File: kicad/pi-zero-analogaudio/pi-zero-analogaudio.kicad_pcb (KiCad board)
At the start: 2 copper layers, 30.5 x 26 mm, 13 parts, among them J1 Audio Out, J2 Pi Connector 2x5 Female, U1 STX-3120-3B

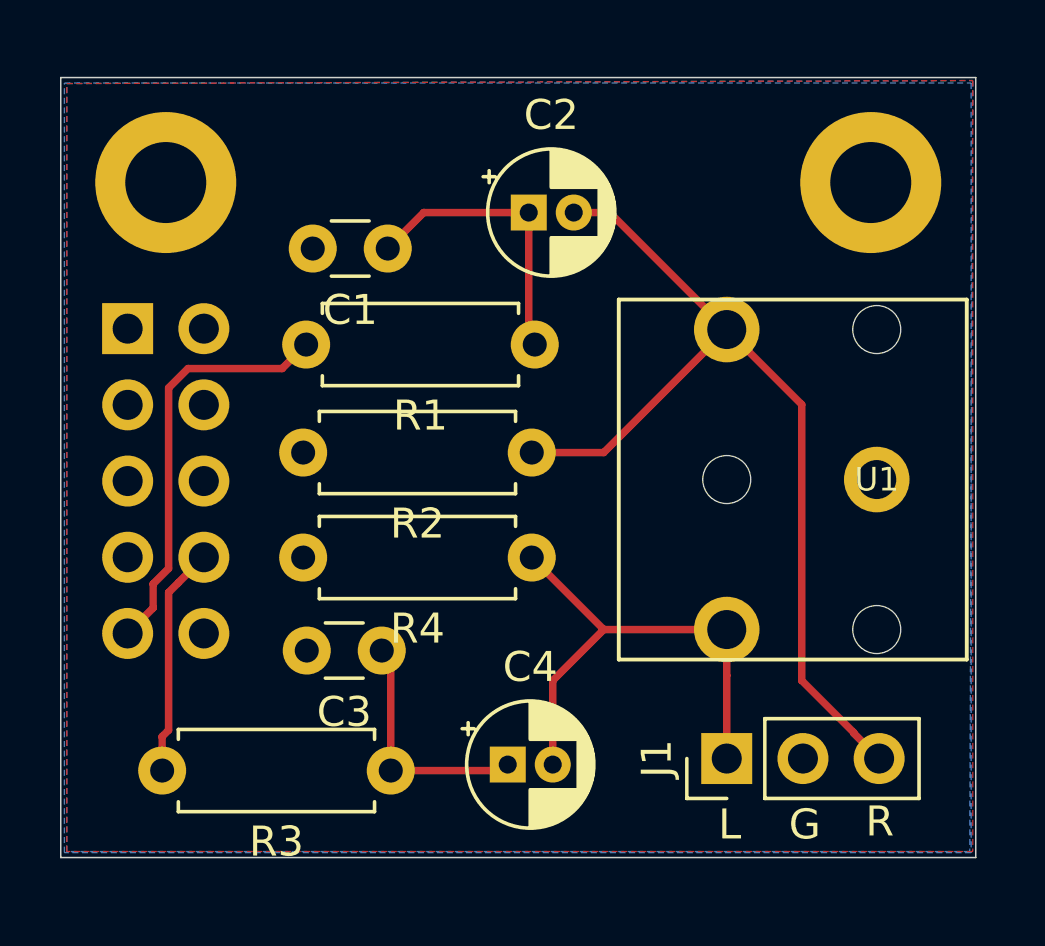
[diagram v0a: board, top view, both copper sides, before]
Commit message: Revision 8: replaced STX3120-3B with STX3120-5B
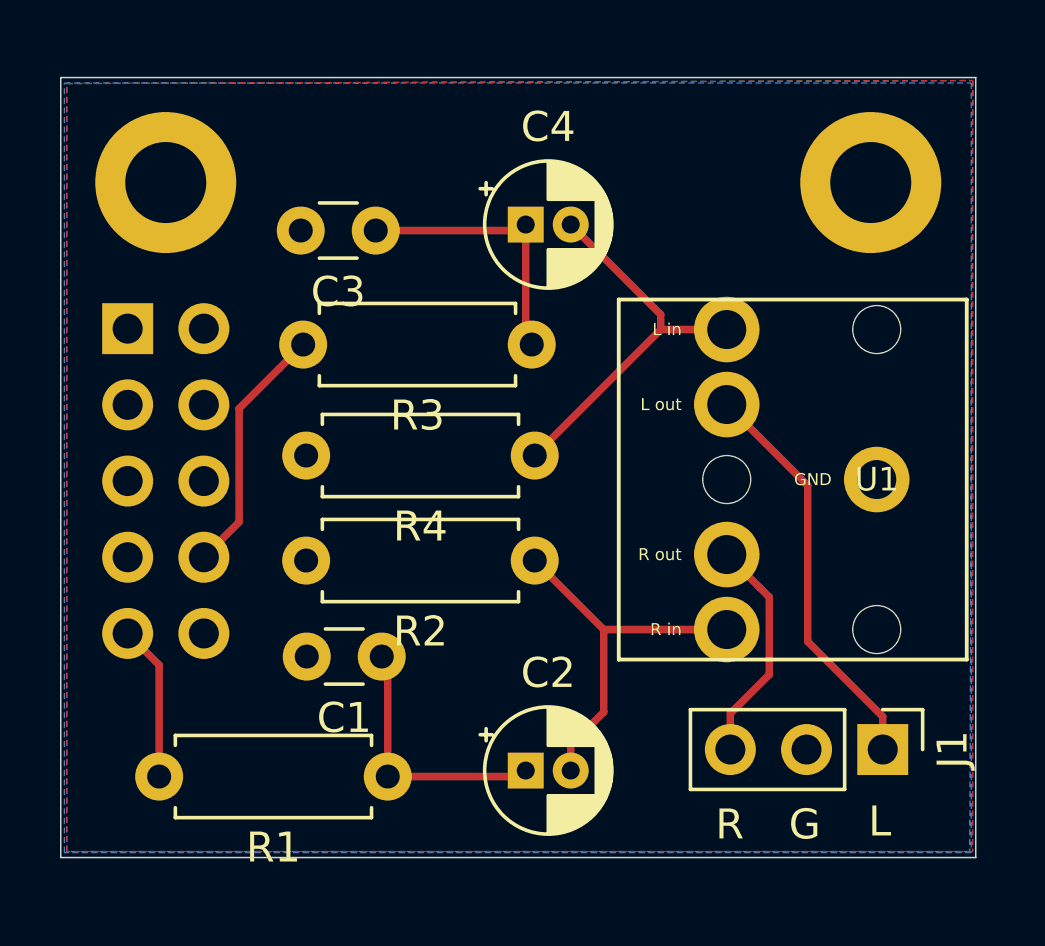
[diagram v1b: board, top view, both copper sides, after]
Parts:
- U1: value STX-3120-3B -> STX-3120-5B; footprint Download:STX-3120 -> Download:STX-3120-5B
- moved C2 18.6 mm to (102.5, 82.1)
- moved C4 18.0 mm to (102.5, 63.9)
- moved R1 15.2 mm to (97.9, 82.3)
- moved R3 15.0 mm to (102.7, 67.9)
- moved C3 14.0 mm to (97.5, 64.1)
- moved C1 13.6 mm to (97.7, 78.3)
- moved J1 5.21 mm to (114.4, 81.4), turned to 270 degrees
- moved R2 3.60 mm to (102.8, 75.1)
- moved R4 3.40 mm to (102.8, 71.6)
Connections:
- J1 pad 1: Net-(C4-Pad2) -> Net-(J1-Pad1)
- J1 pad 3: Net-(C2-Pad2) -> Net-(J1-Pad3)
- U1 pad 2: Net-(C2-Pad2) -> Net-(C4-Pad2)
- U1 pad 5: Net-(C4-Pad2) -> Net-(C2-Pad2)
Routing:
- net Net-(C2-Pad2): track 31.3 -> 12.5 mm
- net Net-(J1-Pad1): track 0.00 -> 13.7 mm
- net Net-(J2-Pad9): track 13.9 -> 5.20 mm
- net Net-(J1-Pad3): track 0.00 -> 7.62 mm
- net Net-(C4-Pad2): track 17.0 -> 12.9 mm
- net Net-(C3-Pad1): track 8.11 -> 9.17 mm
- net Net-(C1-Pad1): track 9.68 -> 8.77 mm
- net Net-(J2-Pad8): track 7.69 -> 8.46 mm
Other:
- board text added: "https://github.com/bablokb/pi-zero-analogaudio"

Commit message: added cutoff
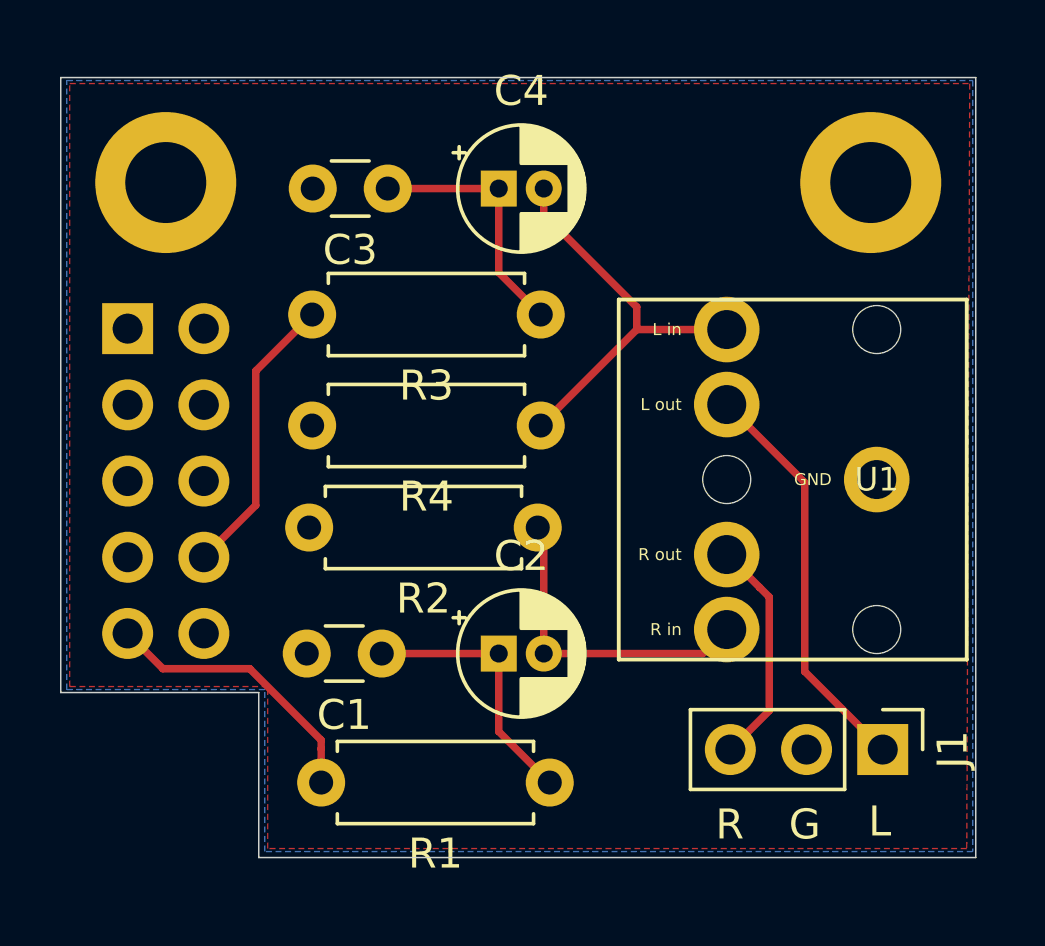
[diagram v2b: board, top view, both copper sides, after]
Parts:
- moved R1 5.40 mm to (103.3, 82.5)
- moved C2 4.00 mm to (101.6, 78.2)
- moved C4 1.50 mm to (101.6, 62.7)
- moved C3 1.46 mm to (97.9, 62.7)
- moved R2 1.10 mm to (102.9, 74.0)
- moved R3 1.04 mm to (103.0, 66.9)
- moved R4 1.02 mm to (103.0, 70.6)
- moved C1 0.10 mm to (97.7, 78.2)
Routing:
- net Net-(J2-Pad9): track 5.20 -> 9.34 mm
- net Net-(C2-Pad2): track 12.5 -> 10.7 mm
- net Net-(C4-Pad2): track 12.9 -> 14.1 mm
- net Net-(J2-Pad8): track 8.46 -> 9.59 mm
- net Net-(C3-Pad1): track 9.17 -> 8.48 mm
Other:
- outline, holes or cut-outs redrawn
- board text added: "Pi-Zero Audio Rev 8"
- board text removed: "Pi-Zero Audio Rev 7"
